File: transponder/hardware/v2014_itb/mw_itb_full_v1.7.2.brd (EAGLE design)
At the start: 96 x 96 mm, 36 parts, among them SW1 SWITCH_SPST-KMT0, SW2 SWITCH_SPST-KMT0

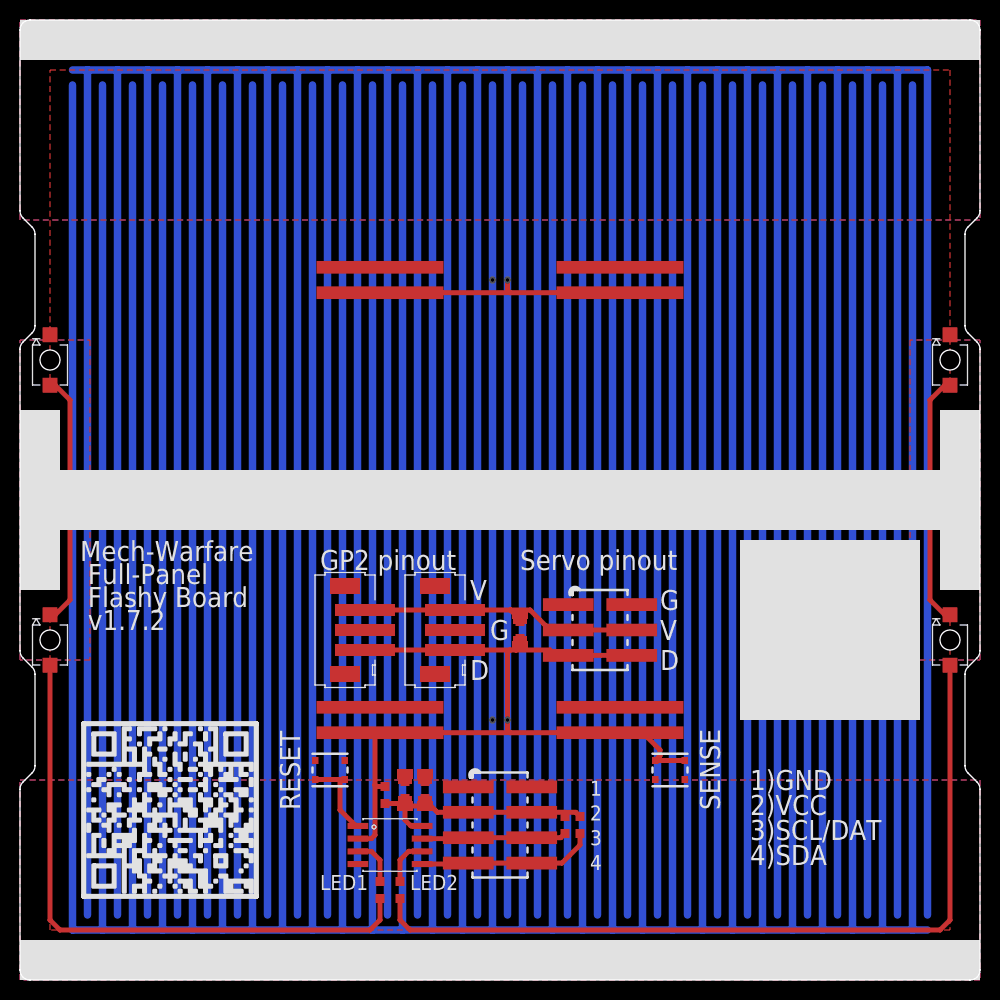
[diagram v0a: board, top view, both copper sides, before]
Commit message: Small updates to mw_itb design files.  Basically changed silkscreen for LEDs and added additional button footprint for slightly larger and significantly less expensive TL3315 pushbuttons from E-Switch.   Silkscreen of C&K Components KMT0 footprint was slightly modified to permit it being nested inside new switch footprint.
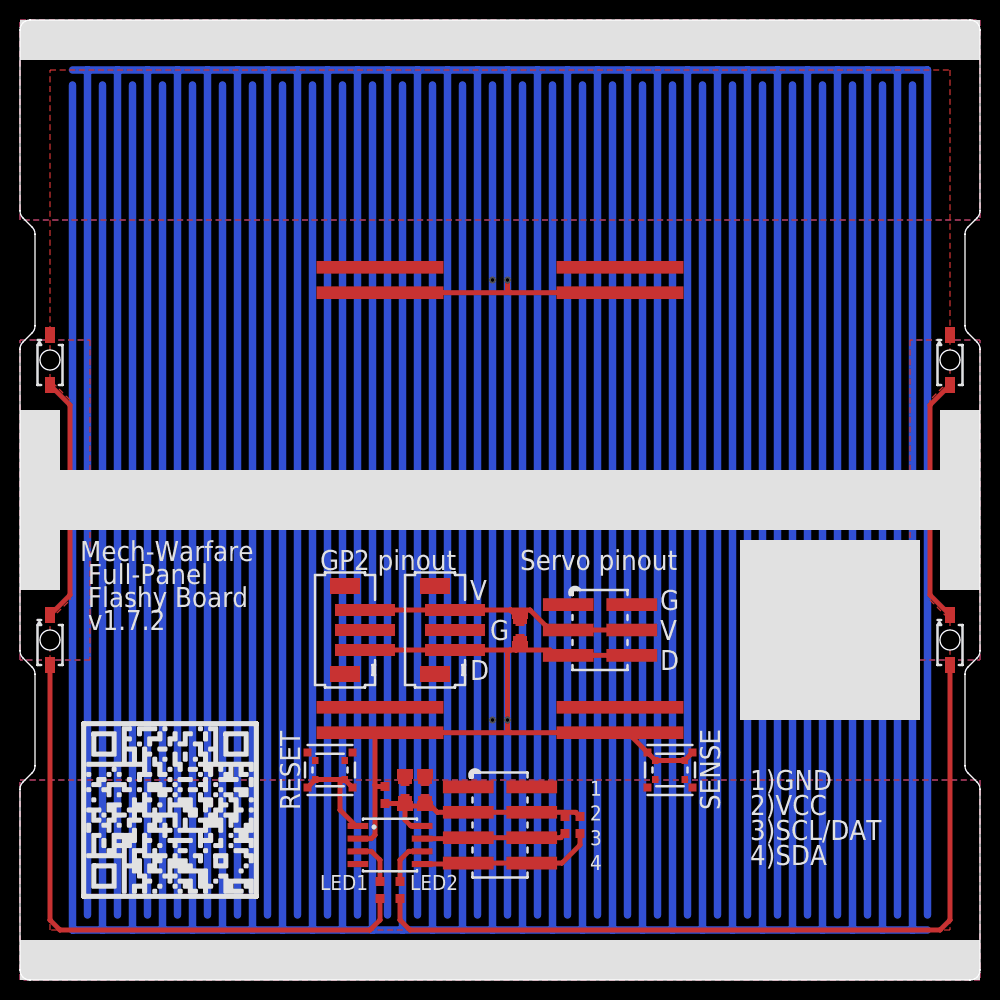
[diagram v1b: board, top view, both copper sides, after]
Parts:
- added SW3, SW4: SWITCH_SPST-TL3315, NaN:SWITCH_TL3315
- SW1, SW2: device NaN:KMT0 -> NaN:SWITCH_KMT0
- turned C1 to 0 degrees
- turned C2 to 0 degrees
- turned C3 to 0 degrees
- turned C4 to 0 degrees
- turned C5 to 0 degrees
- turned C6 to 0 degrees
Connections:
- net !RESET: now also SW3.1@1, SW3.1@2
- net 5V: now also C1.2, C2.2, C3.2, C4.2, C5.2, C6.2; no longer C1.1, C2.1, C3.1, C4.1, C5.1, C6.1
- net GND: now also C1.1, C2.1, C3.1, C4.1, C5.1, C6.1, SW3.2@1, SW3.2@2, SW4.2@1, SW4.2@2; no longer C1.2, C2.2, C3.2, C4.2, C5.2, C6.2
- net SENSE: now also SW4.1@1, SW4.1@2
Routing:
- net !RESET: track 8.89 -> 11.1 mm
- net N$4: track 25.2 -> 24.7 mm
- net N$2: track 25.2 -> 24.7 mm
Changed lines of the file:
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@@
 <element name="RLED1" library="NaN" package="0603_YAGEO" value="" x="36" y="9" rot="R180"/>
 <element name="RLED2" library="NaN" package="0603_YAGEO" value="" x="38" y="9" rot="R180"/>
-<element name="C1" library="NaN" package="1206_YAGEO" value="" x="40.5" y="19" rot="R180"/>
-<element name="C2" library="NaN" package="1206_YAGEO" value="" x="38.5" y="19" rot="R180"/>
+<element name="C1" library="NaN" package="1206_YAGEO" value="" x="40.5" y="19"/>
+<element name="C2" library="NaN" package="1206_YAGEO" value="" x="38.5" y="19"/>
 <element name="U$11" library="NaN" package="IKON_LEARNING_20MIL" value="IKONLEARNING-20MIL" x="15" y="17"/>
 <element name="FSR$1" library="NaN" package="FSR_PAD_88X44_P2B" value="FSR_PAD88X44_P2B" x="48" y="26"/>
 <element name="R1" library="NaN" package="1206_YAGEO" value="" x="50" y="35" rot="R180"/>
 <element name="R2" library="NaN" package="0805_YAGEO" value="" x="50" y="35" rot="R180"/>
-<element name="C3" library="NaN" package="0805_YAGEO" value="" x="40.5" y="19" rot="R180"/>
-<element name="C4" library="NaN" package="0805_YAGEO" value="" x="38.5" y="19" rot="R180"/>
-<element name="C5" library="NaN" package="0603_YAGEO" value="" x="40.5" y="19" rot="R180"/>
-<element name="C6" library="NaN" package="0603_YAGEO" value="" x="38.5" y="19" rot="R180"/>
+<element name="C3" library="NaN" package="0805_YAGEO" value="" x="40.5" y="19"/>
+<element name="C4" library="NaN" package="0805_YAGEO" value="" x="38.5" y="19"/>
+<element name="C5" library="NaN" package="0603_YAGEO" value="" x="40.5" y="19"/>
+<element name="C6" library="NaN" package="0603_YAGEO" value="" x="38.5" y="19"/>
 <element name="R3" library="NaN" package="0603_YAGEO" value="" x="50" y="35" rot="R180"/>
 <element name="R4" library="NaN" package="0603_YAGEO" value="" x="36.5" y="18.5" rot="R180"/>
@@
 <element name="R5" library="NaN" package="0603_YAGEO" value="4.7k" x="54.5" y="15.5" rot="R180"/>
 <element name="R6" library="NaN" package="0603_YAGEO" value="4.7k" x="56" y="15.5" rot="R180"/>
-<element name="SW1" library="NaN" package="KMT0" value="SWITCH_SPST-KMT0" x="31" y="21" rot="R180"/>
-<element name="SW2" library="NaN" package="KMT0" value="SWITCH_SPST-KMT0" x="65" y="21"/>
+<element name="SW1" library="NaN" package="SWITCH_KMT0" value="SWITCH_SPST-KMT0" x="31" y="21" rot="R180"/>
+<element name="SW2" library="NaN" package="SWITCH_KMT0" value="SWITCH_SPST-KMT0" x="65" y="21"/>
 <element name="MCU1" library="NaN" package="SOIC-8_DUAL" value="ATMEL_ATTINY25/45/85(V)-SOIC_DUAL" x="37" y="13.5"/>
 <element name="U$1" library="NaN" package="FSR_0.1&quot;-PITCH_PADS-0.05&quot;X0.5&quot;" value="FSR_PINS" x="60" y="70" rot="R270"/>
@@
 <element name="H3" library="NaN" package="HEADER-0.1&quot;_2X4-SMD-SULLINS" value="HEADER_8P-0.1&quot;_2X4-SMD-SULLINS" x="48" y="15.5" rot="R270"/>
 <element name="H1" library="NaN" package="HEADER-0.1&quot;_2X3-SMD-SULLINS" value="HEADER_6P-0.1&quot;_2X3-SMD-SULLINS" x="58" y="35" rot="R270"/>
+<element name="SW3" library="NaN" package="SWITCH_TL3315" value="SWITCH_SPST-TL3315" x="31" y="21" rot="R180"/>
+<element name="SW4" library="NaN" package="SWITCH_TL3315" value="SWITCH_SPST-TL3315" x="65" y="21"/>
 </elements>
 <signals>
@@
 <contactref element="U$10" pad="P$1"/>
 <contactref element="U$9" pad="P$2"/>
-<contactref element="C1" pad="2"/>
-<contactref element="C2" pad="2"/>
+<contactref element="C1" pad="1"/>
+<contactref element="C2" pad="1"/>
 <contactref element="LED3" pad="K"/>
 <contactref element="LED1" pad="K"/>
 <contactref element="FSR$1" pad="B"/>
-<contactref element="C3" pad="2"/>
-<contactref element="C4" pad="2"/>
-<contactref element="C5" pad="2"/>
-<contactref element="C6" pad="2"/>
+<contactref element="C3" pad="1"/>
+<contactref element="C4" pad="1"/>
+<contactref element="C5" pad="1"/>
+<contactref element="C6" pad="1"/>
 <polygon width="0.5" layer="1" isolate="0.5" thermals="no" rank="2">
 <vertex x="3" y="5"/>
@@
 <contactref element="H1" pad="2"/>
 <contactref element="H1" pad="1"/>
+<contactref element="SW3" pad="2@1"/>
+<contactref element="SW3" pad="2@2"/>
+<contactref element="SW4" pad="2@1"/>
+<contactref element="SW4" pad="2@2"/>
 </signal>
 <signal name="5V">
-<contactref element="C1" pad="1"/>
-<contactref element="C2" pad="1"/>
-<contactref element="C3" pad="1"/>
-<contactref element="C4" pad="1"/>
-<contactref element="C5" pad="1"/>
-<contactref element="C6" pad="1"/>
+<contactref element="C1" pad="2"/>
+<contactref element="C2" pad="2"/>
+<contactref element="C3" pad="2"/>
+<contactref element="C4" pad="2"/>
+<contactref element="C5" pad="2"/>
+<contactref element="C6" pad="2"/>
 <contactref element="R4" pad="1"/>
 <wire x1="38.5" y1="17.4" x2="40.5" y2="17.4" width="0.5" layer="1"/>
@@
 <contactref element="MCU1" pad="1"/>
 <wire x1="33.7875" y1="15.405" x2="33.595" y2="15.405" width="0.5" layer="1"/>
+<contactref element="SW3" pad="1@1"/>
+<contactref element="SW3" pad="1@2"/>
+<wire x1="32.475" y1="20.05" x2="32.475" y2="20.025" width="0.5" layer="1"/>
+<wire x1="32.475" y1="20.025" x2="33.25" y2="19.25" width="0.5" layer="1"/>
+<wire x1="29.525" y1="20.05" x2="29.525" y2="20.025" width="0.5" layer="1"/>
+<wire x1="29.525" y1="20.025" x2="28.75" y2="19.25" width="0.5" layer="1"/>
 </signal>
 <signal name="SCL">
@@
 <contactref element="SW2" pad="1@1"/>
 <wire x1="66.475" y1="21.95" x2="63.525" y2="21.95" width="0.5" layer="1"/>
-<wire x1="60" y1="24.73" x2="62.27" y2="24.73" width="0.5" layer="1"/>
-<wire x1="62.27" y1="24.73" x2="64" y2="23" width="0.5" layer="1"/>
-<wire x1="64" y1="23" x2="64" y2="22.425" width="0.5" layer="1"/>
-<wire x1="64" y1="22.425" x2="63.525" y2="21.95" width="0.5" layer="1"/>
 <contactref element="MCU1" pad="2"/>
 <contactref element="JST2" pad="1"/>
@@
 <wire x1="54.825" y1="32.46" x2="53.54" y2="32.46" width="0.5" layer="1"/>
 <wire x1="53.54" y1="32.46" x2="53" y2="33" width="0.5" layer="1"/>
+<contactref element="SW4" pad="1@1"/>
+<contactref element="SW4" pad="1@2"/>
+<wire x1="66.475" y1="21.95" x2="66.475" y2="21.975" width="0.5" layer="1"/>
+<wire x1="66.475" y1="21.975" x2="67.25" y2="22.75" width="0.5" layer="1"/>
+<wire x1="63.525" y1="21.95" x2="63.525" y2="21.975" width="0.5" layer="1"/>
+<wire x1="63.525" y1="21.975" x2="62.75" y2="22.75" width="0.5" layer="1"/>
+<wire x1="60" y1="24.73" x2="60.77" y2="24.73" width="0.5" layer="1"/>
+<wire x1="60.77" y1="24.73" x2="62.75" y2="22.75" width="0.5" layer="1"/>
 </signal>
 <signal name="LED2">
@@
 <wire x1="35" y1="5" x2="4" y2="5" width="0.5" layer="1"/>
 <wire x1="4" y1="5" x2="3" y2="6" width="0.5" layer="1"/>
-<wire x1="3" y1="6" x2="3" y2="31.475" width="0.5" layer="1"/>
+<wire x1="3" y1="6" x2="3" y2="31.5" width="0.5" layer="1"/>
 </signal>
 <signal name="N$2">
 <contactref element="LED1" pad="A"/>
 <contactref element="LED2" pad="K"/>
-<wire x1="3" y1="36.525" x2="3.525" y2="36.525" width="0.5" layer="1"/>
-<wire x1="3.525" y1="36.525" x2="5" y2="38" width="0.5" layer="1"/>
-<wire x1="5" y1="38" x2="5" y2="58" width="0.5" layer="1"/>
-<wire x1="5" y1="58" x2="3.525" y2="59.475" width="0.5" layer="1"/>
-<wire x1="3.525" y1="59.475" x2="3" y2="59.475" width="0.5" layer="1"/>
+<wire x1="5" y1="38.5" x2="5" y2="57.5" width="0.5" layer="1"/>
+<wire x1="5" y1="38.5" x2="3" y2="36.5" width="0.5" layer="1"/>
+<wire x1="5" y1="57.5" x2="3" y2="59.5" width="0.5" layer="1"/>
 </signal>
 <signal name="N$3">
@@
 <wire x1="39" y1="5" x2="92" y2="5" width="0.5" layer="1"/>
 <wire x1="92" y1="5" x2="93" y2="6" width="0.5" layer="1"/>
-<wire x1="93" y1="6" x2="93" y2="31.475" width="0.5" layer="1"/>
+<wire x1="93" y1="6" x2="93" y2="31.5" width="0.5" layer="1"/>
 </signal>
 <signal name="N$4">
 <contactref element="LED4" pad="K"/>
 <contactref element="LED3" pad="A"/>
-<wire x1="93" y1="36.525" x2="92.475" y2="36.525" width="0.5" layer="1"/>
-<wire x1="92.475" y1="36.525" x2="91" y2="38" width="0.5" layer="1"/>
-<wire x1="91" y1="38" x2="91" y2="58" width="0.5" layer="1"/>
-<wire x1="91" y1="58" x2="92.475" y2="59.475" width="0.5" layer="1"/>
-<wire x1="92.475" y1="59.475" x2="93" y2="59.475" width="0.5" layer="1"/>
+<wire x1="91" y1="38.5" x2="91" y2="57.5" width="0.5" layer="1"/>
+<wire x1="91" y1="57.5" x2="93" y2="59.5" width="0.5" layer="1"/>
+<wire x1="91" y1="38.5" x2="93" y2="36.5" width="0.5" layer="1"/>
 </signal>
 <signal name="LED1">
@@
 </signal>
 </signals>
+<errors>
+</errors>
 </board>
 </drawing>
